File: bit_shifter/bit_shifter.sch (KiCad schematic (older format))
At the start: 7 parts

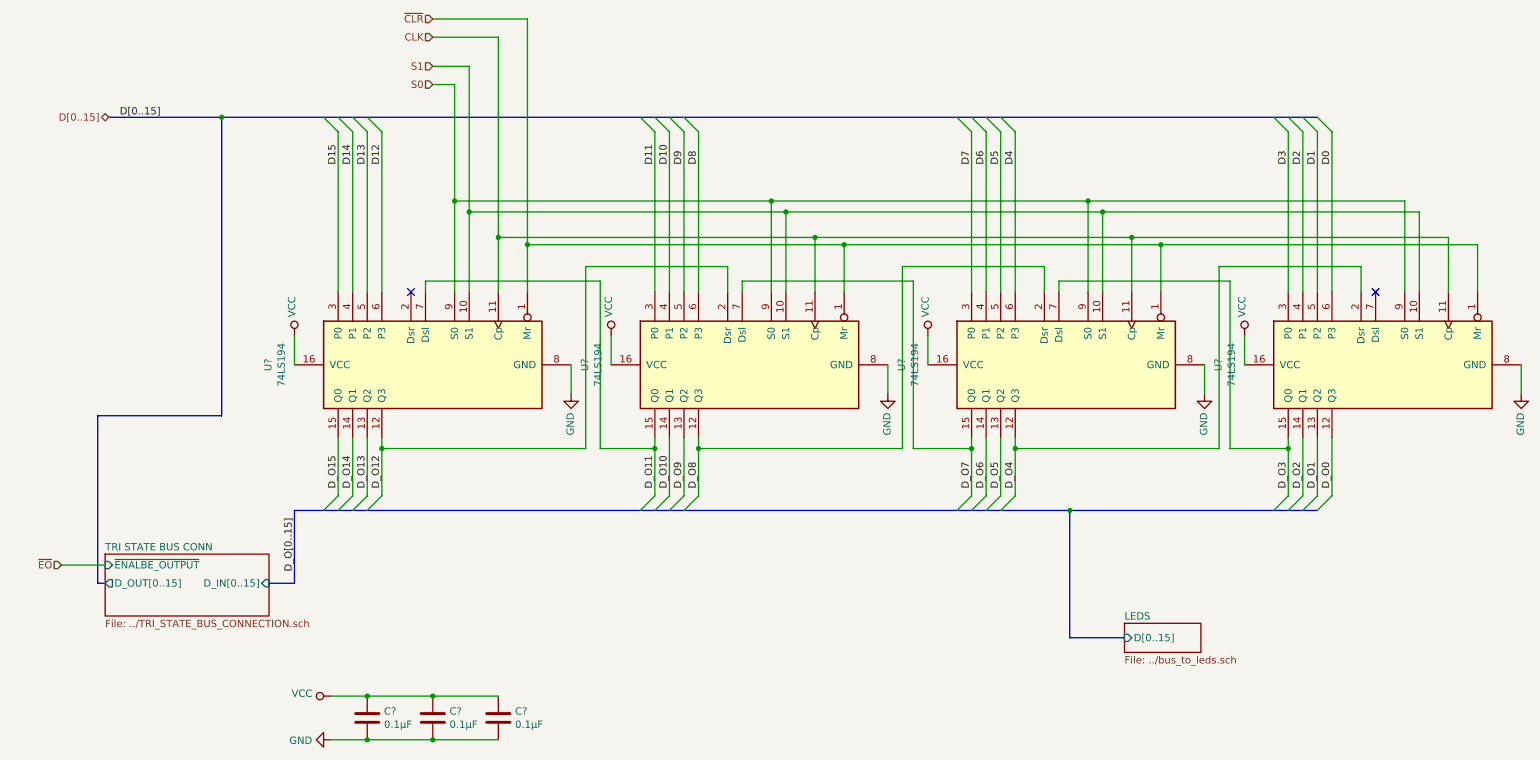
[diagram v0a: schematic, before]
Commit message: connect cu and start creating material csv
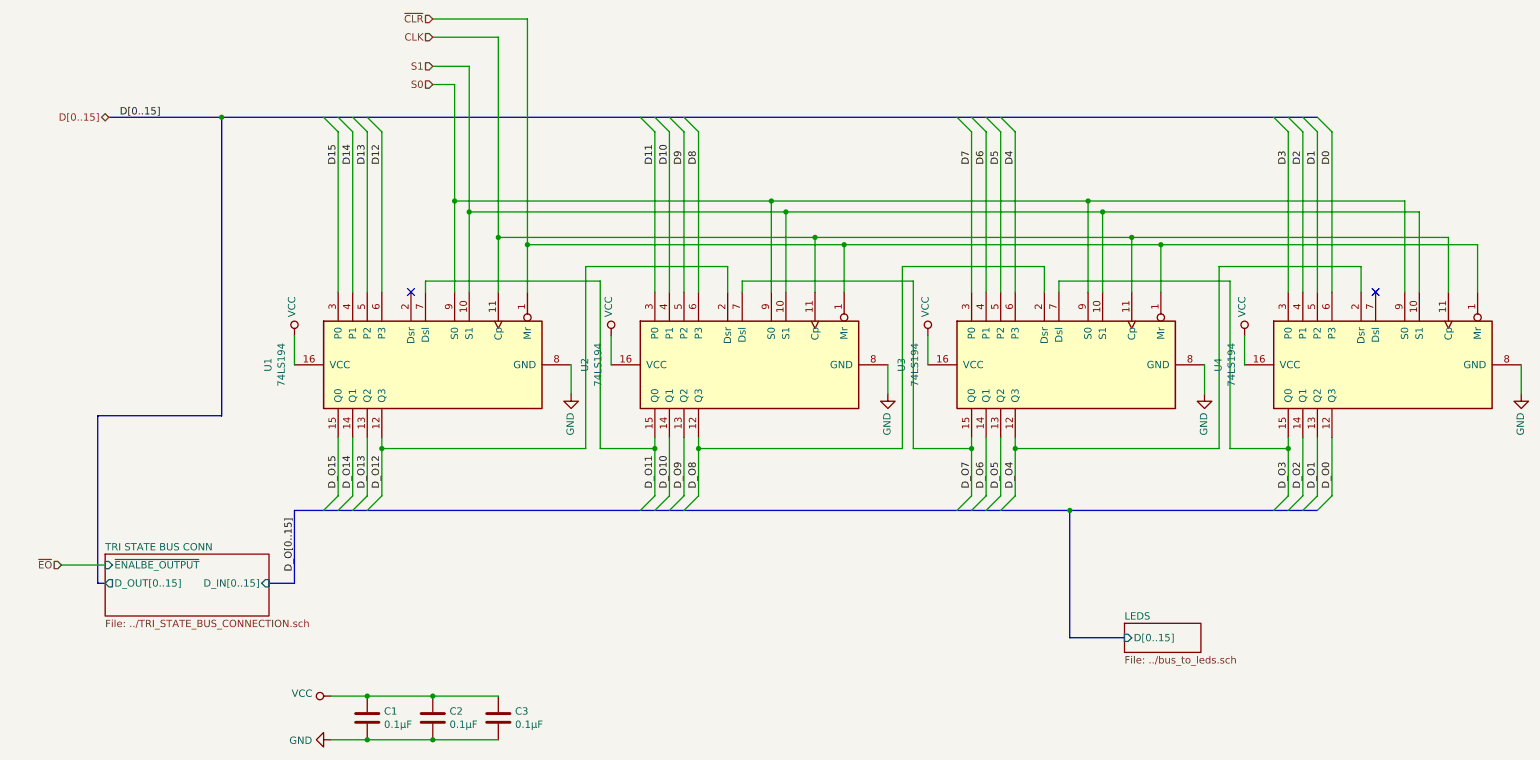
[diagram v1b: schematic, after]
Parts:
- gave numbers to parts that had none: 7
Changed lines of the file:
@@
 EESchema Schematic File Version 4
-LIBS:computer-cache
+LIBS:bit_shifter_pcb-cache
 EELAYER 30 0
 EELAYER END
 $Descr A4 11693 8268
 encoding utf-8
-Sheet 2 29
+Sheet 2 6
 Title ""
 Date ""
@@
 $EndDescr
 $Comp
-L power:VCC #PWR?
+L power:VCC #PWR07
 U 1 1 5F291FD2
 P 6700 2825
-F 0 "#PWR?" H 6700 2675 50  0001 C CNN
+F 0 "#PWR07" H 6700 2675 50  0001 C CNN
 F 1 "VCC" V 6718 2952 50  0000 L CNN
 F 2 "" H 6700 2825 50  0001 C CNN
@@
 	6700 2825 6700 3025
 $Comp
-L power:GND #PWR?
+L power:GND #PWR08
 U 1 1 5F291FD9
 P 8600 3225
-F 0 "#PWR?" H 8600 2975 50  0001 C CNN
+F 0 "#PWR08" H 8600 2975 50  0001 C CNN
 F 1 "GND" V 8605 3097 50  0000 R CNN
 F 2 "" H 8600 3225 50  0001 C CNN
@@
 	8600 3225 8600 3025
 $Comp
-L 74xx:74LS194 U?
+L 74xx:74LS194 U2
 U 1 1 5F29EF10
 P 5425 3025
-F 0 "U?" H 5425 4106 50  0000 C CNN
+F 0 "U2" H 5425 4106 50  0000 C CNN
 F 1 "74LS194" H 5425 4015 50  0000 C CNN
 F 2 "Package_DIP:DIP-16_W7.62mm_LongPads" H 5425 3025 50  0001 C CNN
@@
 $EndComp
 $Comp
-L power:VCC #PWR?
+L power:VCC #PWR05
 U 1 1 5F29EF16
 P 4525 2825
-F 0 "#PWR?" H 4525 2675 50  0001 C CNN
+F 0 "#PWR05" H 4525 2675 50  0001 C CNN
 F 1 "VCC" V 4543 2952 50  0000 L CNN
 F 2 "" H 4525 2825 50  0001 C CNN
@@
 	4525 2825 4525 3025
 $Comp
-L power:GND #PWR?
+L power:GND #PWR06
 U 1 1 5F29EF1D
 P 6425 3225
-F 0 "#PWR?" H 6425 2975 50  0001 C CNN
+F 0 "#PWR06" H 6425 2975 50  0001 C CNN
 F 1 "GND" V 6430 3097 50  0000 R CNN
 F 2 "" H 6425 3225 50  0001 C CNN
@@
 	6425 3225 6425 3025
 $Comp
-L 74xx:74LS194 U?
+L 74xx:74LS194 U1
 U 1 1 5F29EF24
 P 3250 3025
-F 0 "U?" H 3250 4106 50  0000 C CNN
+F 0 "U1" H 3250 4106 50  0000 C CNN
 F 1 "74LS194" H 3250 4015 50  0000 C CNN
 F 2 "Package_DIP:DIP-16_W7.62mm_LongPads" H 3250 3025 50  0001 C CNN
@@
 $EndComp
 $Comp
-L power:VCC #PWR?
+L power:VCC #PWR01
 U 1 1 5F29EF2A
 P 2350 2825
-F 0 "#PWR?" H 2350 2675 50  0001 C CNN
+F 0 "#PWR01" H 2350 2675 50  0001 C CNN
 F 1 "VCC" V 2368 2952 50  0000 L CNN
 F 2 "" H 2350 2825 50  0001 C CNN
@@
 	2350 2825 2350 3025
 $Comp
-L power:GND #PWR?
+L power:GND #PWR04
 U 1 1 5F29EF31
 P 4250 3225
-F 0 "#PWR?" H 4250 2975 50  0001 C CNN
+F 0 "#PWR04" H 4250 2975 50  0001 C CNN
 F 1 "GND" V 4255 3097 50  0000 R CNN
 F 2 "" H 4250 3225 50  0001 C CNN
@@
 	4250 3225 4250 3025
 $Comp
-L 74xx:74LS194 U?
+L 74xx:74LS194 U3
 U 1 1 5F291FCC
 P 7600 3025
-F 0 "U?" H 7600 4106 50  0000 C CNN
+F 0 "U3" H 7600 4106 50  0000 C CNN
 F 1 "74LS194" H 7600 4015 50  0000 C CNN
 F 2 "Package_DIP:DIP-16_W7.62mm_LongPads" H 7600 3025 50  0001 C CNN
@@
 	10775 3225 10775 3025
 $Comp
-L power:GND #PWR?
+L power:GND #PWR010
 U 1 1 5F28A3EB
 P 10775 3225
-F 0 "#PWR?" H 10775 2975 50  0001 C CNN
+F 0 "#PWR010" H 10775 2975 50  0001 C CNN
 F 1 "GND" V 10780 3097 50  0000 R CNN
 F 2 "" H 10775 3225 50  0001 C CNN
@@
 	8875 2825 8875 3025
 $Comp
-L power:VCC #PWR?
+L power:VCC #PWR09
 U 1 1 5F288FC3
 P 8875 2825
-F 0 "#PWR?" H 8875 2675 50  0001 C CNN
+F 0 "#PWR09" H 8875 2675 50  0001 C CNN
 F 1 "VCC" V 8893 2952 50  0000 L CNN
 F 2 "" H 8875 2825 50  0001 C CNN
@@
 	5325 2350 5325 2525
 $Comp
-L 74xx:74LS194 U?
+L 74xx:74LS194 U4
 U 1 1 5F2881CF
 P 9775 3025
-F 0 "U?" H 9775 4106 50  0000 C CNN
+F 0 "U4" H 9775 4106 50  0000 C CNN
 F 1 "74LS194" H 9775 4015 50  0000 C CNN
 F 2 "Package_DIP:DIP-16_W7.62mm_LongPads" H 9775 3025 50  0001 C CNN
@@
 D_O[0..15]
 $Comp
-L Device:C C?
+L Device:C C1
 U 1 1 5F3F0346
 P 2850 5450
-F 0 "C?" H 2965 5496 50  0000 L CNN
+F 0 "C1" H 2965 5496 50  0000 L CNN
 F 1 "0.1µF" H 2965 5405 50  0000 L CNN
 F 2 "Capacitor_THT:C_Disc_D4.3mm_W1.9mm_P5.00mm" H 2888 5300 50  0001 C CNN
@@
 $EndComp
 $Comp
-L Device:C C?
+L Device:C C2
 U 1 1 5F3F8444
 P 3300 5450
-F 0 "C?" H 3415 5496 50  0000 L CNN
+F 0 "C2" H 3415 5496 50  0000 L CNN
 F 1 "0.1µF" H 3415 5405 50  0000 L CNN
 F 2 "Capacitor_THT:C_Disc_D4.3mm_W1.9mm_P5.00mm" H 3338 5300 50  0001 C CNN
@@
 $EndComp
 $Comp
-L Device:C C?
+L Device:C C3
 U 1 1 5F3F844A
 P 3750 5450
-F 0 "C?" H 3865 5496 50  0000 L CNN
+F 0 "C3" H 3865 5496 50  0000 L CNN
 F 1 "0.1µF" H 3865 5405 50  0000 L CNN
 F 2 "Capacitor_THT:C_Disc_D4.3mm_W1.9mm_P5.00mm" H 3788 5300 50  0001 C CNN
@@
 	3300 5300 2850 5300
 $Comp
-L power:VCC #PWR?
+L power:VCC #PWR02
 U 1 1 5F401180
 P 2600 5300
-F 0 "#PWR?" H 2600 5150 50  0001 C CNN
+F 0 "#PWR02" H 2600 5150 50  0001 C CNN
 F 1 "VCC" V 2618 5427 50  0000 L CNN
 F 2 "" H 2600 5300 50  0001 C CNN
@@
 	3300 5600 2850 5600
 $Comp
-L power:GND #PWR?
+L power:GND #PWR03
 U 1 1 5F405CE8
 P 2600 5600
-F 0 "#PWR?" H 2600 5350 50  0001 C CNN
+F 0 "#PWR03" H 2600 5350 50  0001 C CNN
 F 1 "GND" V 2605 5472 50  0000 R CNN
 F 2 "" H 2600 5600 50  0001 C CNN

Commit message: Commit uncomitted changes. no clue what I had done last time
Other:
- note added: "TODO ground?"
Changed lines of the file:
@@
 EESchema Schematic File Version 4
-LIBS:bit_shifter_pcb-cache
+LIBS:computer-cache
 EELAYER 30 0
 EELAYER END
 $Descr A4 11693 8268
 encoding utf-8
-Sheet 2 6
+Sheet 26 36
 Title ""
 Date ""
@@
 Wire Bus Line
 	1850 1325 9375 1325
+Text Notes 9775 2450 0    50   ~ 0
+TODO ground?
+Text Notes 3150 2375 0    50   ~ 0
+TODO ground?
 $EndSCHEMATC
